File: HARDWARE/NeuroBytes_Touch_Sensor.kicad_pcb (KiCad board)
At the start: 2 copper layers, 52.3 x 35.1 mm, 27 parts, among them P1 JST_GH_5-pos, P6 CONN_01X04, P7 CONN_01X04, Q1 MMBT3904, Q2 MMBT3904, Q3 MMBT3904, SW1 SW_PUSH, SW2 SW_SNAP_ACTION, U1 STM32L011Gx, U2 3v3 LDO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

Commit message: generated fab and BOM files
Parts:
- removed U3: RClamp0503F, KiCad_Footprints:ZF_SMD_SOT-353
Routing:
- net IDENTIFY: track 12.7 -> 2.37 mm
- net INPUT: track 38.1 -> 34.7 mm, vias 3 -> 2
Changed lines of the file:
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@@
 (kicad_pcb (version 4) (host pcbnew 4.0.7-e2-6376~58~ubuntu14.04.1)
   (general
-    (links 77)
+    (links 73)
     (no_connects 0)
     (area 44.899999 43.8 175.798574 152.84)
     (thickness 1.6)
     (drawings 212)
-    (tracks 245)
+    (tracks 231)
     (zones 0)
-    (modules 27)
-    (nets 40)
+    (modules 26)
+    (nets 39)
   )
   (page A)
@@
     (visible_elements FFFFFF7F)
     (pcbplotparams
-      (layerselection 0x201fc_80000001)
+      (layerselection 0x211fc_80000001)
       (usegerberextensions false)
       (excludeedgelayer true)
@@
       (drillshape 0)
       (scaleselection 1)
-      (outputdirectory /home/zach/Desktop/))
+      (outputdirectory ""))
   )
   (net 0 "")
@@
   (net 37 SWDIO)
   (net 38 SWCLK)
-  (net 39 "Net-(U3-Pad4)")
   (net_class Default "This is the default net class."
     (clearance 0.2)
@@
     (add_net "Net-(U1-Pad3)")
     (add_net "Net-(U2-Pad4)")
-    (add_net "Net-(U3-Pad4)")
     (add_net RESET)
     (add_net SWCLK)
@@
     )
   )
-  (module KiCad_Footprints:ZF_SMD_SOT-353 (layer B.Cu)
-    (at 119.57 81.54 180)
-    (fp_text reference U3 (at 0 -7.3 180) (layer B.SilkS) hide
-      (effects (font (size 1 1) (thickness 0.15)) (justify mirror))
-    )
-    (fp_text value RClamp0503F (at 0 4 180) (layer B.Fab) hide
-      (effects (font (size 1 1) (thickness 0.15)) (justify mirror))
-    )
-    (fp_circle (center -1.2 -0.8) (end -1.2 -0.6) (layer B.SilkS) (width 0.1))
-    (fp_line (start -1 0.6) (end 1 0.6) (layer B.SilkS) (width 0.1))
-    (fp_line (start -1 -0.6) (end -1 0.6) (layer B.SilkS) (width 0.1))
-    (fp_line (start 1 -0.6) (end -1 -0.6) (layer B.SilkS) (width 0.1))
-    (fp_line (start 1 0.6) (end 1 -0.6) (layer B.SilkS) (width 0.1))
-    (pad 1 smd rect (at -0.65 -1 180) (size 0.3 0.8) (layers B.Cu B.Paste B.Mask)
-      (net 14 INPUT))
-    (pad 2 smd rect (at 0 -1 180) (size 0.3 0.8) (layers B.Cu B.Paste B.Mask)
-      (net 2 GND))
-    (pad 3 smd rect (at 0.65 -1 180) (size 0.3 0.8) (layers B.Cu B.Paste B.Mask)
-      (net 13 IDENTIFY))
-    (pad 4 smd rect (at 0.65 1 180) (size 0.3 0.8) (layers B.Cu B.Paste B.Mask)
-      (net 39 "Net-(U3-Pad4)"))
-    (pad 5 smd rect (at -0.65 1 180) (size 0.3 0.8) (layers B.Cu B.Paste B.Mask)
-      (net 3 +3V3))
-  )
   (module KiCad_Footprints:ZF_LOGO_Touch_Sensor (layer F.Cu)
     (at 126.49 69.46)
+    (attr smd)
     (fp_text reference G*** (at 0 0) (layer F.SilkS) hide
       (effects (font (thickness 0.3)))
@@
       (xy -0.065316 -1.268257) (xy 0.284937 -1.240064)) (layer F.Mask) (width 0.01))
   )
+  (gr_text "TOUCH SENSORY NEURON" (at 125.2 82.4) (layer F.SilkS)
+    (effects (font (size 1 1) (thickness 0.14) italic))
+  )
   (gr_line (start 94.37 98.74) (end 89.37 98.74) (layer F.Fab) (width 0.2))
   (gr_line (start 91.87 96.24) (end 91.87 101.24) (layer F.Fab) (width 0.2))
@@
   (gr_text "V-SCORE PARALLEL ENDS" (at 87 45) (layer F.Fab)
     (effects (font (size 1.5 1.5) (thickness 0.3)))
-  )
-  (gr_text "TOUCH SENSORY NEURON" (at 125.2 82.4) (layer F.SilkS)
-    (effects (font (size 1 1) (thickness 0.14) italic))
   )
   (gr_text NeuroBytes (at 125.2 80.3) (layer F.Cu)
@@
   (via (at 139.5 82.4) (size 0.6) (drill 0.4) (layers F.Cu B.Cu) (net 2))
   (segment (start 129.824264 74.775736) (end 130.524264 75.475736) (width 0.2) (layer B.Cu) (net 2))
+  (segment (start 117.569999 80.529999) (end 121.380001 80.529999) (width 0.5) (layer B.Cu) (net 3))
+  (segment (start 121.380001 80.529999) (end 121.67 80.24) (width 0.5) (layer B.Cu) (net 3))
   (via (at 117.569999 80.529999) (size 0.6) (drill 0.4) (layers F.Cu B.Cu) (net 3))
   (segment (start 108.6 89.1) (end 108.6 85.91) (width 0.5) (layer F.Cu) (net 3))
   (segment (start 108.6 85.91) (end 113.980001 80.529999) (width 0.5) (layer F.Cu) (net 3))
   (segment (start 113.980001 80.529999) (end 117.569999 80.529999) (width 0.5) (layer F.Cu) (net 3))
-  (segment (start 119.57 79.64) (end 120.22 80.29) (width 0.5) (layer B.Cu) (net 3))
-  (segment (start 118.459998 79.64) (end 119.57 79.64) (width 0.5) (layer B.Cu) (net 3))
-  (segment (start 117.569999 80.529999) (end 118.459998 79.64) (width 0.5) (layer B.Cu) (net 3))
-  (segment (start 120.22 80.29) (end 120.22 80.54) (width 0.5) (layer B.Cu) (net 3))
-  (segment (start 120.22 80.54) (end 121.37 80.54) (width 0.5) (layer B.Cu) (net 3))
   (segment (start 121.37 80.54) (end 121.67 80.24) (width 0.5) (layer B.Cu) (net 3))
   (segment (start 123.07 80.94) (end 122.37 80.94) (width 0.5) (layer B.Cu) (net 3))
@@
   (segment (start 129.257716 78.113604) (end 130.763604 78.113604) (width 0.2) (layer B.Cu) (net 12))
   (segment (start 130.763604 78.113604) (end 130.9 78.25) (width 0.2) (layer B.Cu) (net 12))
-  (segment (start 118.92 83.14) (end 118.92 82.54) (width 0.2) (layer B.Cu) (net 13))
-  (segment (start 119.582165 84.04) (end 118.92 83.377835) (width 0.2) (layer B.Cu) (net 13))
-  (segment (start 127.136396 81.507716) (end 124.604112 84.04) (width 0.2) (layer B.Cu) (net 13))
-  (segment (start 124.604112 84.04) (end 119.582165 84.04) (width 0.2) (layer B.Cu) (net 13))
-  (segment (start 118.92 83.377835) (end 118.92 83.14) (width 0.2) (layer B.Cu) (net 13))
   (segment (start 128.058644 82.429964) (end 127.136396 81.507716) (width 0.2) (layer B.Cu) (net 13))
   (segment (start 129.120359 82.429964) (end 128.058644 82.429964) (width 0.2) (layer B.Cu) (net 13))
-  (segment (start 120.744998 81.540001) (end 120.744998 82.015002) (width 0.2) (layer B.Cu) (net 14))
-  (segment (start 120.744998 82.015002) (end 120.22 82.54) (width 0.2) (layer B.Cu) (net 14))
-  (segment (start 120.744998 81.540001) (end 120.744998 82.714998) (width 0.2) (layer F.Cu) (net 14))
+  (segment (start 110.87 84.54) (end 112.17 83.24) (width 0.2) (layer F.Cu) (net 14))
+  (segment (start 123.07 83.24) (end 112.17 83.24) (width 0.2) (layer F.Cu) (net 14))
   (segment (start 124.331321 83.04) (end 126.146447 81.224874) (width 0.2) (layer B.Cu) (net 14))
   (segment (start 123.07 83.24) (end 124.131321 83.24) (width 0.2) (layer B.Cu) (net 14))
   (segment (start 124.131321 83.24) (end 124.331321 83.04) (width 0.2) (layer B.Cu) (net 14))
-  (segment (start 120.744998 82.714998) (end 121.27 83.24) (width 0.2) (layer F.Cu) (net 14))
-  (segment (start 121.27 83.24) (end 123.07 83.24) (width 0.2) (layer F.Cu) (net 14))
   (via (at 123.07 83.24) (size 0.6) (drill 0.4) (layers F.Cu B.Cu) (net 14))
-  (segment (start 110.87 84.54) (end 113.869999 81.540001) (width 0.2) (layer F.Cu) (net 14))
-  (segment (start 113.869999 81.540001) (end 120.744998 81.540001) (width 0.2) (layer F.Cu) (net 14))
-  (via (at 120.744998 81.540001) (size 0.6) (drill 0.4) (layers F.Cu B.Cu) (net 14))
   (segment (start 109.27 86.14) (end 110.87 84.54) (width 0.2) (layer F.Cu) (net 14))
   (segment (start 109.27 86.54) (end 109.27 86.14) (width 0.2) (layer F.Cu) (net 14))

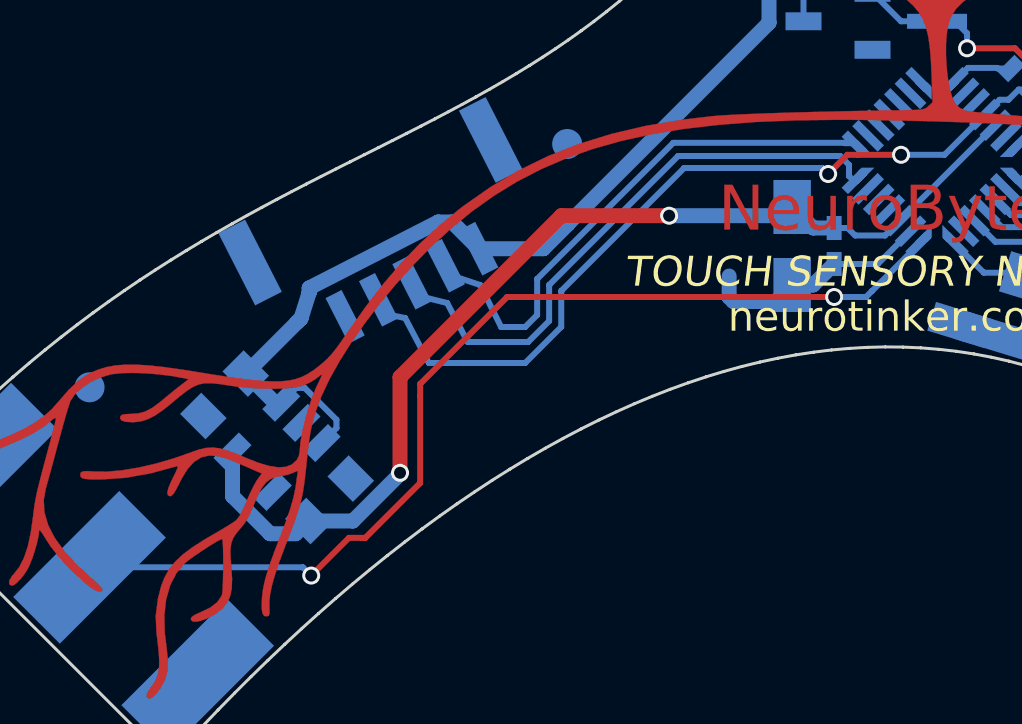
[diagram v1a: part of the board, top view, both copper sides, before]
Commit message: updated 0603 and 1206 footprints. minor routing fix. added placement pdf.
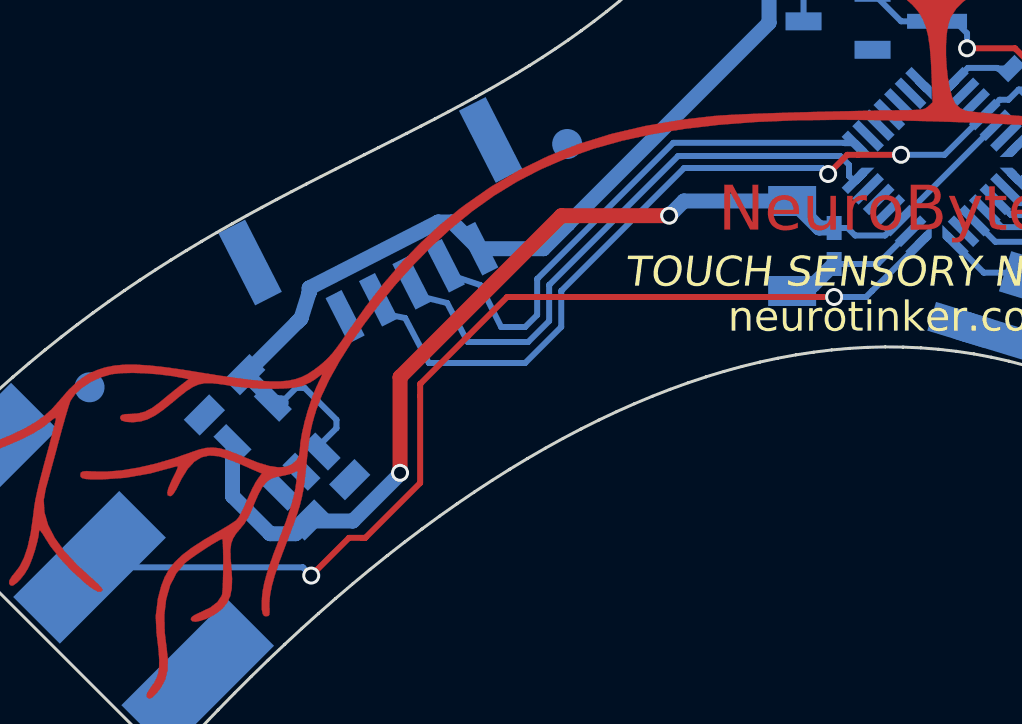
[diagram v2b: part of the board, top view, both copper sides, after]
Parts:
- C1, C4: footprint KiCad_Footprints:ZF_SMD_NonPol_0603 -> Capacitors_SMD:C_0603_HandSoldering
- C2: footprint KiCad_Footprints:ZF_SMD_nonpol_1206 -> Capacitors_SMD:C_1206
- turned U2 to 225 degrees
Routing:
- net GND: track 25.6 -> 22.5 mm
- net Net-(U2-Pad4): track 0.00 -> 1.48 mm
- net +5V: track 71.8 -> 70.9 mm
- net +3V3: track 36.2 -> 35.3 mm

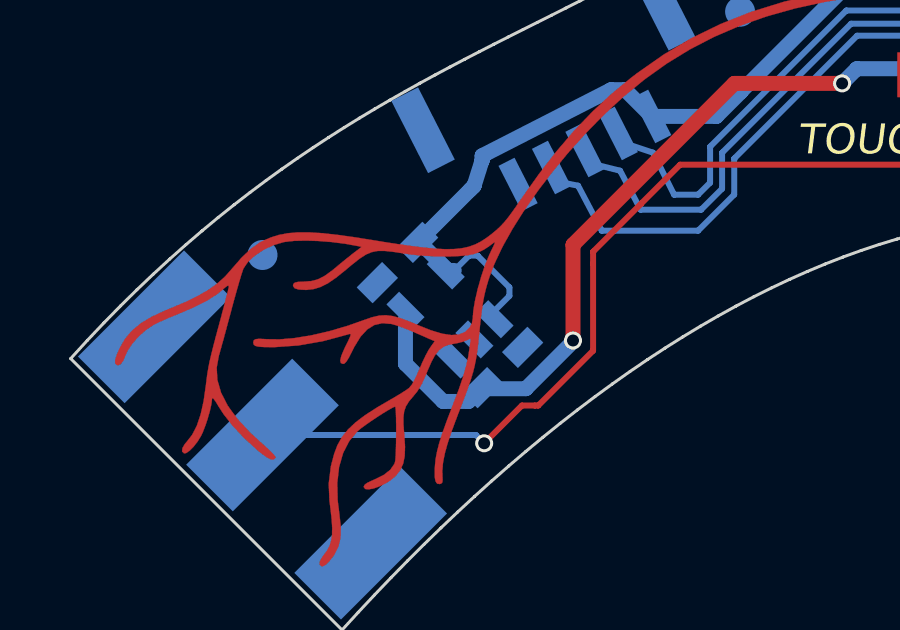
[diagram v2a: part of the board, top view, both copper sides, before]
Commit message: fixed #*$&ing regulator rotation that caused delays and resulted in much scrap
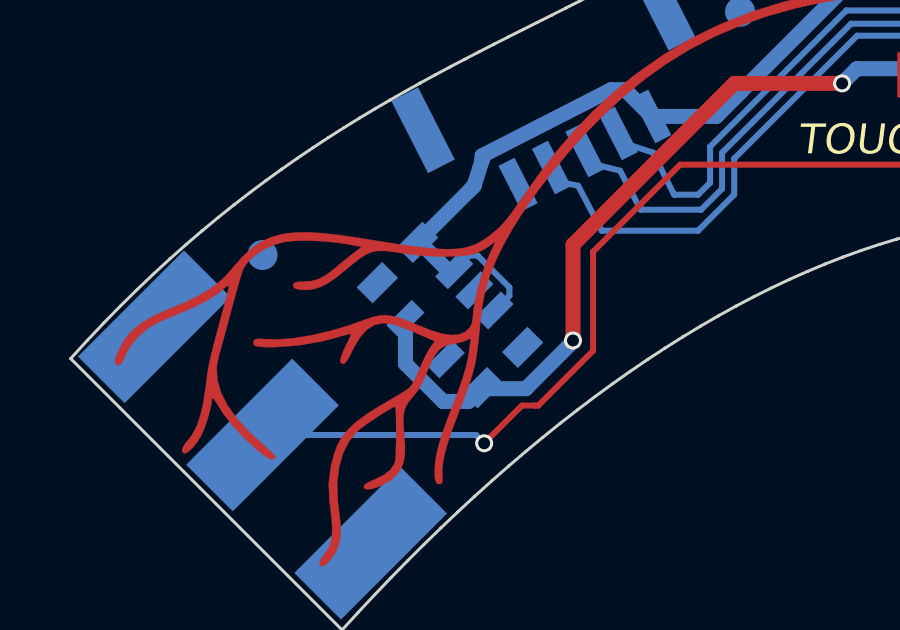
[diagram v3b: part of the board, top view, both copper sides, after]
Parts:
- turned U2 to 315 degrees
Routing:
- net Net-(U2-Pad4): track 1.48 -> 0.00 mm
- net +5V: track 70.9 -> 71.8 mm
- net +3V3: track 35.3 -> 35.9 mm
